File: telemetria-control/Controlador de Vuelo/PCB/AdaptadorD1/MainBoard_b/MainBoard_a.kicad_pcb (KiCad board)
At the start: 2 copper layers, 43.2 x 43.2 mm, 7 parts, among them J1 Conn_01x04, Q1 BC548, U1 WeMos_mini

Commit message: Add files via upload
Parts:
- removed BT1: Battery_Cell, Componentes:Holder2032
- added ?: , kicad:logo, F.Cu at (154.9, 76.8)
- added ?: , kicad:logo, B.Cu at (140.3, 78.7)
- added J2: Conn_01x05, Connector_PinHeader_2.54mm:PinHeader_1x05_P2.54mm_Vertical, F.Cu at (152.4, 85.1)
- added J3: Conn_01x02, Connector_PinHeader_2.54mm:PinHeader_1x02_P2.54mm_Vertical, F.Cu at (146.1, 74.9)
- added J4: Conn_01x08, Connector_PinHeader_2.54mm:PinHeader_1x08_P2.54mm_Vertical, F.Cu at (131.4, 102.9)
- added J5: Conn_01x08, Connector_PinHeader_2.54mm:PinHeader_1x08_P2.54mm_Vertical, F.Cu at (167.0, 86.4)
- added R3: 10K, Resistor_SMD:R_1206_3216Metric, B.Cu at (140.3, 96.5)
- added U2: 4066, Package_SO:SOIC-14_3.9x8.7mm_P1.27mm, B.Cu at (147.3, 94.0)
- BZ1: footprint Buzzers_Beepers:Buzzer_12x9.5RM7.6 -> Buzzer_Beeper:Buzzer_12x9.5RM7.6; moved to B.Cu
- J1: footprint Pin_Headers:Pin_Header_Angled_1x04_Pitch2.54mm -> Connector_PinHeader_2.54mm:PinHeader_1x04_P2.54mm_Vertical
- Q1: footprint TO_SOT_Packages_THT:TO-92_Molded_Narrow -> Package_TO_SOT_THT:TO-92L_Wide
- R1, R2: footprint Resistors_THT:R_Axial_DIN0207_L6.3mm_D2.5mm_P7.62mm_Horizontal -> Resistor_SMD:R_1206_3216Metric
- U1: footprint wemos_d1_mini:D1_mini_board -> Module:WEMOS_D1_mini_light
- moved Q1 73.9 mm to (160.0, 108.0)
- moved R1 60.1 mm to (161.9, 98.4), turned to 90 degrees
- moved U1 59.6 mm to (135.9, 85.1)
- moved J1 54.5 mm to (151.1, 113.7), turned to 270 degrees
- moved BZ1 47.4 mm to (162.6, 83.2), turned to 270 degrees
- moved R2 43.2 mm to (160.7, 79.4)
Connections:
- U1 pad 10: Net-(U1-Pad10) -> Analog
- U1 pad 11: Net-(U1-Pad11) -> X_Sel
- U1 pad 12: Net-(U1-Pad12) -> Y_Sel
- U1 pad 13: Net-(U1-Pad13) -> Z_Sel
- U1 pad 15: Net-(U1-Pad15) -> Buzzer
- U1 pad 3: Buzzer -> Net-(J4-Pad6)
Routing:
- net 3v3: track 69.5 -> 113.1 mm
- net Analog: track 0.00 -> 36.6 mm
- net Net-(J2-Pad3): track 0.00 -> 28.8 mm, vias 0 -> 2
- net Z_Sel: track 0.00 -> 28.8 mm, vias 0 -> 2
- net SDA: track 9.42 -> 32.0 mm
- net Net-(J2-Pad4): track 0.00 -> 21.4 mm
- net X_Sel: track 0.00 -> 18.3 mm
- net Y_Sel: track 0.00 -> 17.7 mm
- net SCL: track 13.8 -> 24.5 mm
- net Net-(BZ1-Pad2): track 25.3 -> 35.6 mm
- net Net-(J5-Pad3): track 0.00 -> 10.0 mm
- net Net-(J5-Pad8): track 0.00 -> 8.78 mm
- net GND: track 54.6 -> 63.1 mm
- net Net-(Q1-Pad2): track 6.90 -> 13.3 mm
- net Net-(J2-Pad2): track 0.00 -> 5.11 mm
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- added copper zone on F.Cu, net GND
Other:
- board size 43.2 x 43.2 mm -> 45 x 45 mm
- net class Default: trace_width 0.95 -> 0.6

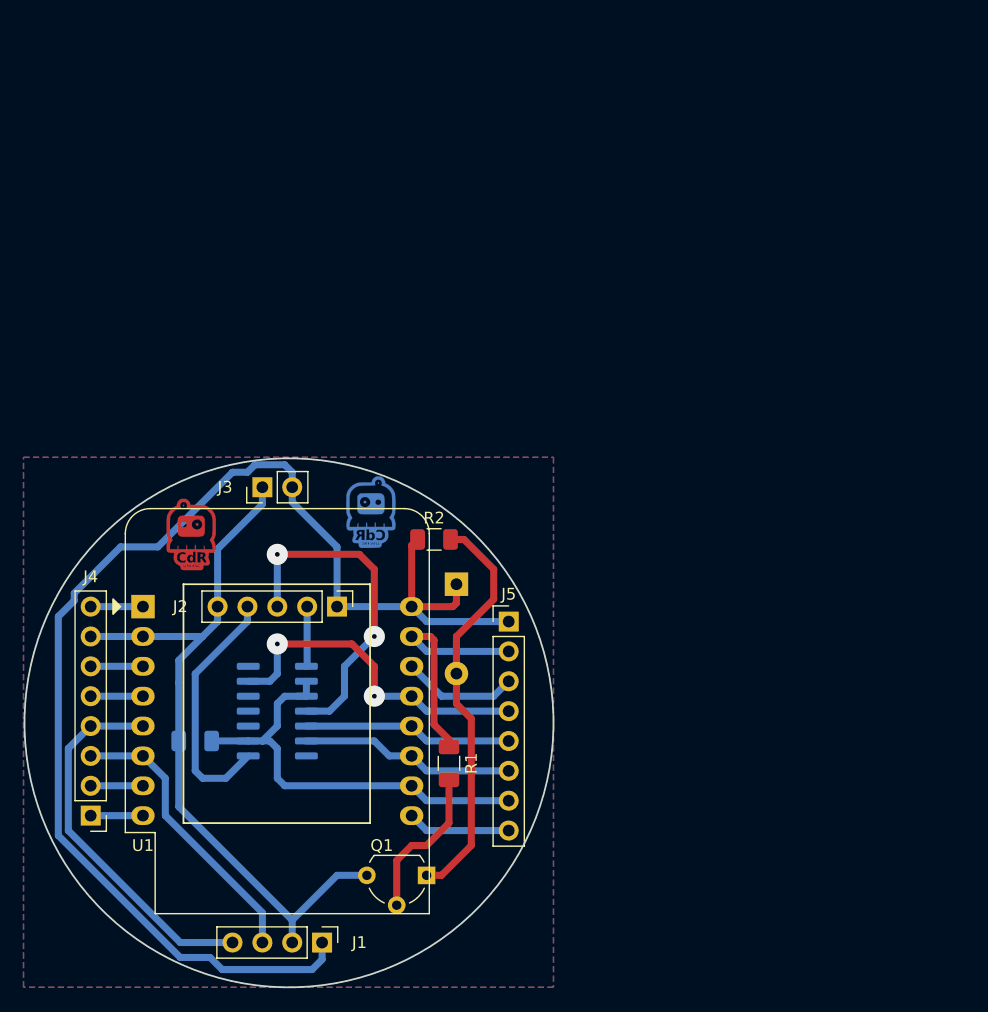
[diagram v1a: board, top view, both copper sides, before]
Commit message: Error: se hizo una placa nueva arriba del proyecto de una vieja, Solucion:se restauro la version mas vieja y se creo la placa nueva en otra carpeta
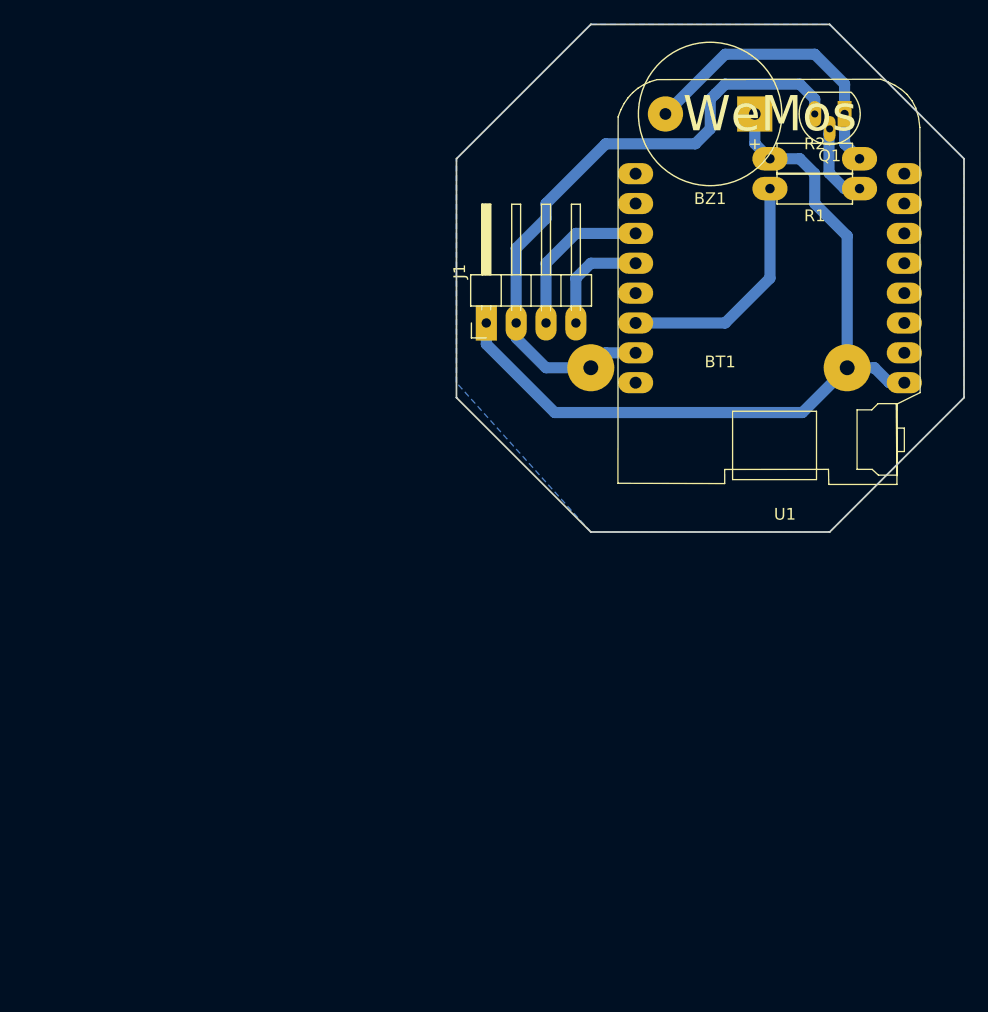
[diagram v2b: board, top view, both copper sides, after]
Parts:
- removed ? (x2): , kicad:logo
- removed J2: Conn_01x05, Connector_PinHeader_2.54mm:PinHeader_1x05_P2.54mm_Vertical
- removed J3: Conn_01x02, Connector_PinHeader_2.54mm:PinHeader_1x02_P2.54mm_Vertical
- removed J4, J5: Conn_01x08, Connector_PinHeader_2.54mm:PinHeader_1x08_P2.54mm_Vertical
- removed R3: 10K, Resistor_SMD:R_1206_3216Metric
- removed U2: 4066, Package_SO:SOIC-14_3.9x8.7mm_P1.27mm
- added BT1: Battery_Cell, Componentes:Holder2032, F.Cu at (185.0, 64.8)
- BZ1: footprint Buzzer_Beeper:Buzzer_12x9.5RM7.6 -> Buzzers_Beepers:Buzzer_12x9.5RM7.6; moved to F.Cu
- J1: footprint Connector_PinHeader_2.54mm:PinHeader_1x04_P2.54mm_Vertical -> Pin_Headers:Pin_Header_Angled_1x04_Pitch2.54mm
- Q1: footprint Package_TO_SOT_THT:TO-92L_Wide -> TO_SOT_Packages_THT:TO-92_Molded_Narrow
- R1, R2: footprint Resistor_SMD:R_1206_3216Metric -> Resistors_THT:R_Axial_DIN0207_L6.3mm_D2.5mm_P7.62mm_Horizontal
- U1: footprint Module:WEMOS_D1_mini_light -> wemos_d1_mini:D1_mini_board
- moved Q1 73.9 mm to (195.6, 43.2)
- moved R1 60.1 mm to (196.8, 49.5), turned to 180 degrees
- moved U1 59.6 mm to (189.2, 58.4)
- moved J1 54.5 mm to (165.1, 61.0), turned to 90 degrees
- moved BZ1 47.4 mm to (187.9, 43.2), turned to 180 degrees
- moved R2 43.2 mm to (189.2, 47.0)
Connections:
- U1 pad 10: Analog -> Net-(U1-Pad10)
- U1 pad 11: X_Sel -> Net-(U1-Pad11)
- U1 pad 12: Y_Sel -> Net-(U1-Pad12)
- U1 pad 13: Z_Sel -> Net-(U1-Pad13)
- U1 pad 15: Buzzer -> Net-(U1-Pad15)
- U1 pad 3: Net-(J4-Pad6) -> Buzzer
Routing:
- net 3v3: track 113.1 -> 69.5 mm
- net Analog: track 36.6 -> 0.00 mm
- net Net-(J2-Pad3): track 28.8 -> 0.00 mm, vias 2 -> 0
- net Z_Sel: track 28.8 -> 0.00 mm, vias 2 -> 0
- net SDA: track 32.0 -> 9.42 mm
- net Net-(J2-Pad4): track 21.4 -> 0.00 mm
- net X_Sel: track 18.3 -> 0.00 mm
- net Y_Sel: track 17.7 -> 0.00 mm
- net SCL: track 24.5 -> 13.8 mm
- net Net-(BZ1-Pad2): track 35.6 -> 25.3 mm
- net Net-(U1-Pad14): track 10.0 -> 0.00 mm
- net Net-(U1-Pad9): track 8.78 -> 0.00 mm
- net GND: track 63.1 -> 54.6 mm
- net Net-(Q1-Pad2): track 13.3 -> 6.90 mm
- net Net-(J2-Pad2): track 5.11 -> 0.00 mm
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- removed copper zone on F.Cu, net GND
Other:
- board size 45 x 45 mm -> 43.2 x 43.2 mm
- net class Default: trace_width 0.6 -> 0.95
